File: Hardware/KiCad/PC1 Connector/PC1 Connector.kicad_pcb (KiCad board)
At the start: 2 copper layers, 35 x 17.5 mm, 9 parts, among them J1 Conn_01x09, J2 PCUI Port

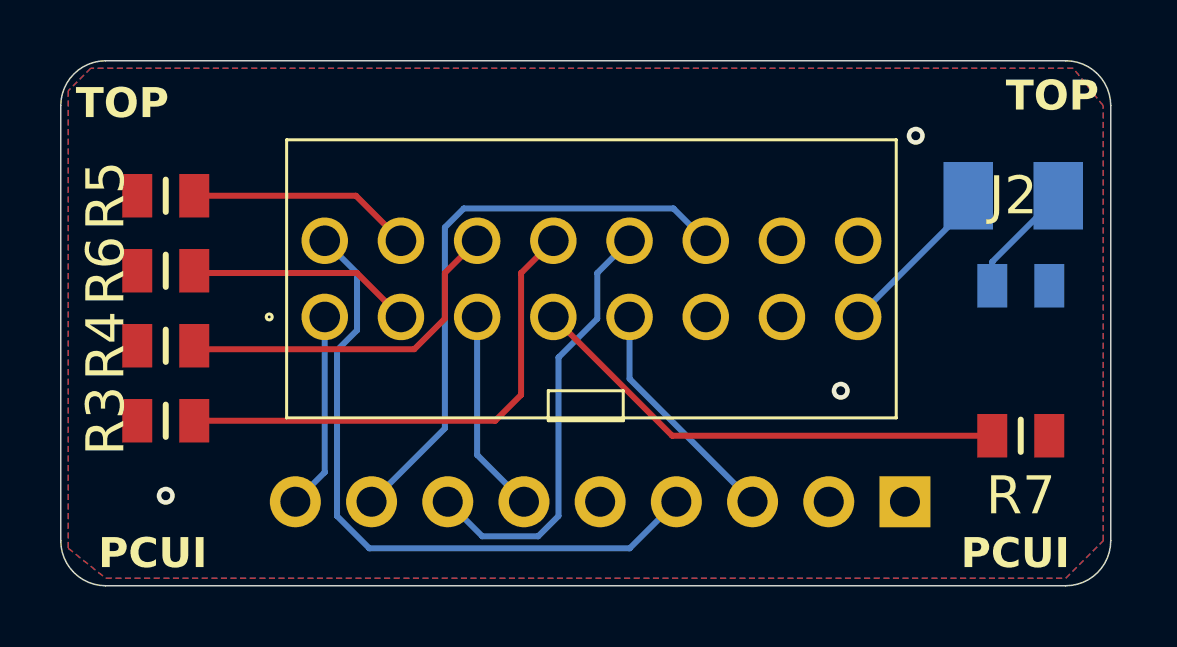
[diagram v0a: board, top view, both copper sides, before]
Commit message: Updated owners manual and PC-1 Connector.
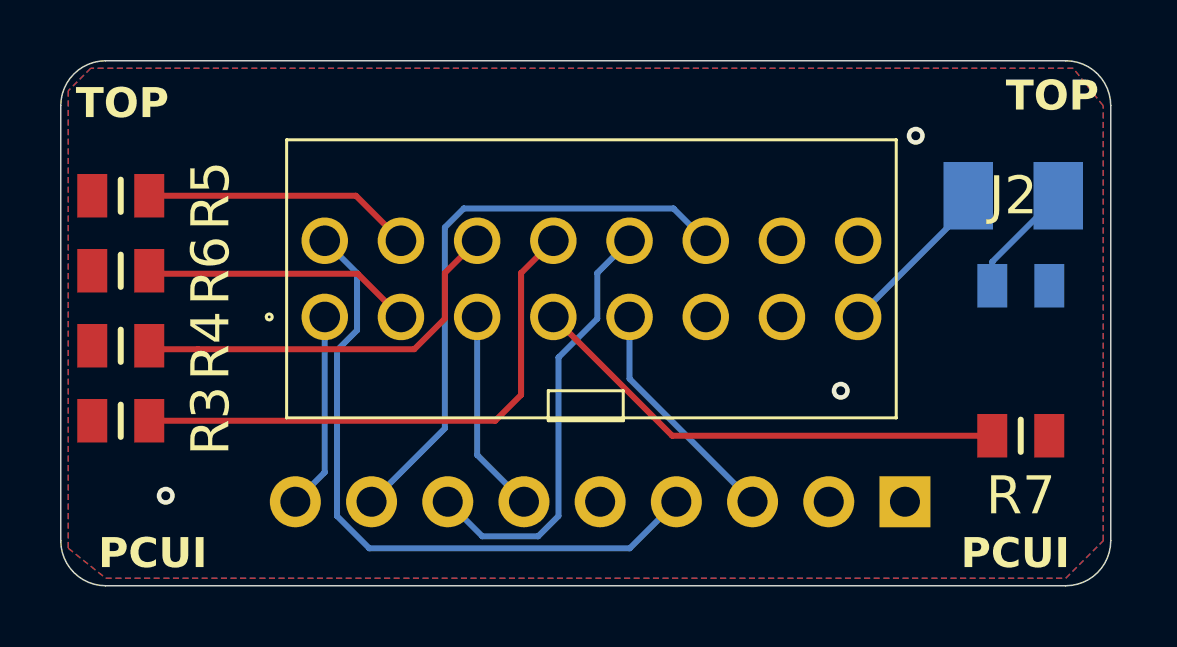
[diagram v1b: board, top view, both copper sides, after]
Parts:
- moved R3 1.50 mm to (107.0, 99.5)
- moved R4 1.50 mm to (107.0, 97.0)
- moved R5 1.50 mm to (107.0, 92.0)
- moved R6 1.50 mm to (107.0, 94.5)
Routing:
- net Net-(J2-Pad8): track 16.8 -> 18.3 mm
- net Net-(J2-Pad6): track 11.9 -> 13.4 mm
- net Net-(J2-Pad4): track 7.51 -> 9.01 mm
- net Net-(J2-Pad3): track 7.53 -> 9.03 mm
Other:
- board text added: "N1UGK REV 1.1"
- board text removed: "N1UGK REV 1.0"
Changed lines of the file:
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@@
 	(footprint "footprints:RESC2013X65N"
 		(layer "F.Cu")
-		(at 108.5 97)
+		(at 107 97)
 		(descr "WCR0805")
 		(tags "Resistor")
 		(property "Reference" "R4"
-			(at -2 0 90)
+			(at 3 0 90)
 			(layer "F.SilkS")
 			(effects
@@
 		)
 		(fp_text user "${REFERENCE}"
-			(at -2 0 90)
+			(at 3 0 90)
 			(layer "F.Fab")
 			(effects
@@
 	(footprint "footprints:RESC2013X65N"
 		(layer "F.Cu")
-		(at 108.5 99.5)
+		(at 107 99.5)
 		(descr "WCR0805")
 		(tags "Resistor")
 		(property "Reference" "R3"
-			(at -2 0 90)
+			(at 3 0 90)
 			(layer "F.SilkS")
 			(effects
@@
 		)
 		(fp_text user "${REFERENCE}"
-			(at -2 0 90)
+			(at 3 0 90)
 			(layer "F.Fab")
 			(effects
@@
 	(footprint "footprints:RESC2013X65N"
 		(layer "F.Cu")
-		(at 108.5 94.5 180)
+		(at 107 94.5 180)
 		(descr "WCR0805")
 		(tags "Resistor")
 		(property "Reference" "R6"
-			(at 2 0 90)
+			(at -3 0 90)
 			(layer "F.SilkS")
 			(effects
@@
 		)
 		(fp_text user "${REFERENCE}"
-			(at 2 0 90)
+			(at -3 0 90)
 			(layer "F.Fab")
 			(effects
@@
 	(footprint "footprints:RESC2013X65N"
 		(layer "F.Cu")
-		(at 108.5 92)
+		(at 107 92)
 		(descr "WCR0805")
 		(tags "Resistor")
 		(property "Reference" "R5"
-			(at -2 0 90)
+			(at 3 0 90)
 			(layer "F.SilkS")
 			(effects
@@
 		)
 		(fp_text user "${REFERENCE}"
-			(at -2 0 90)
+			(at 3 0 90)
 			(layer "F.Fab")
 			(effects
@@
 		(tags "Resistor")
 		(property "Reference" "R1"
-			(at 0 0 0)
+			(at 0 -2.5 0)
 			(layer "B.SilkS")
 			(effects
@@
 		)
 		(fp_text user "${REFERENCE}"
-			(at 0 0 0)
+			(at 0 -2.5 0)
 			(layer "B.Fab")
 			(effects
@@
 		(tags "LED")
 		(property "Reference" "LED1"
-			(at 0 0 0)
+			(at 2.75 -3.5 90)
 			(layer "B.SilkS")
 			(effects
@@
 		)
 		(fp_text user "${REFERENCE}"
-			(at 0 0 0)
+			(at 2.75 -3.5 90)
 			(layer "B.Fab")
 			(effects
@@
 		)
 	)
-	(gr_text "N1UGK REV 1.0"
+	(gr_text "N1UGK REV 1.1"
 		(at 107 90.25 90)
 		(layer "B.SilkS")
@@
 	)
 	(segment
+		(start 120.344 98.637694)
+		(end 120.344 94.576)
+		(width 0.2)
+		(layer "F.Cu")
+		(net 3)
+	)
+	(segment
 		(start 120.344 94.576)
 		(end 121.42 93.5)
@@
 	)
 	(segment
-		(start 109.45 99.5)
+		(start 107.95 99.5)
 		(end 119.481694 99.5)
 		(width 0.2)
@@
 	)
 	(segment
-		(start 120.344 98.637694)
-		(end 120.344 94.576)
-		(width 0.2)
-		(layer "F.Cu")
-		(net 3)
-	)
-	(segment
-		(start 109.45 92)
+		(start 116.34 93.5)
 		(end 114.84 92)
 		(width 0.2)
@@
 	(segment
 		(start 114.84 92)
-		(end 116.34 93.5)
+		(end 107.95 92)
 		(width 0.2)
 		(layer "F.Cu")
@@
 	)
 	(segment
+		(start 109.566 97.116)
+		(end 108.066 97.116)
+		(width 0.2)
+		(layer "F.Cu")
+		(net 6)
+	)
+	(segment
 		(start 117.804 96.097694)
 		(end 117.804 94.576)
@@
 	)
 	(segment
-		(start 109.45 97)
-		(end 109.566 97.116)
+		(start 108.066 97.116)
+		(end 107.95 97)
 		(width 0.2)
 		(layer "F.Cu")
@@
 	)
 	(segment
-		(start 109.526 94.576)
-		(end 114.876 94.576)
+		(start 107.95 94.5)
+		(end 108.05 94.6)
 		(width 0.2)
 		(layer "F.Cu")
@@
 	)
 	(segment
-		(start 114.876 94.576)
-		(end 116.34 96.04)
+		(start 108.05 94.6)
+		(end 114.9 94.6)
 		(width 0.2)
 		(layer "F.Cu")
@@
 	)
 	(segment
-		(start 109.45 94.5)
-		(end 109.526 94.576)
+		(start 114.9 94.6)
+		(end 116.34 96.04)
 		(width 0.2)
 		(layer "F.Cu")
